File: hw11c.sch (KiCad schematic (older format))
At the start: 68 parts, among them Q1 KX-7_12MHZ, SW1 BUTT1, SW2 BUTT2, X1 ~RESET, X10 PIO2.8, X11 PIO1.4, X12 ADC3, X13 PIO0.8, X14 PIO0.9, X15 MAT0, X16 PIO0.6, X17 PIO0.7, X2 SWCLK, X3 SWDIO, X4 SSEL1, X5 SCK1, X6 MISO1, X7 MOSI1, X8 PIO2.6, X9 PIO2.7

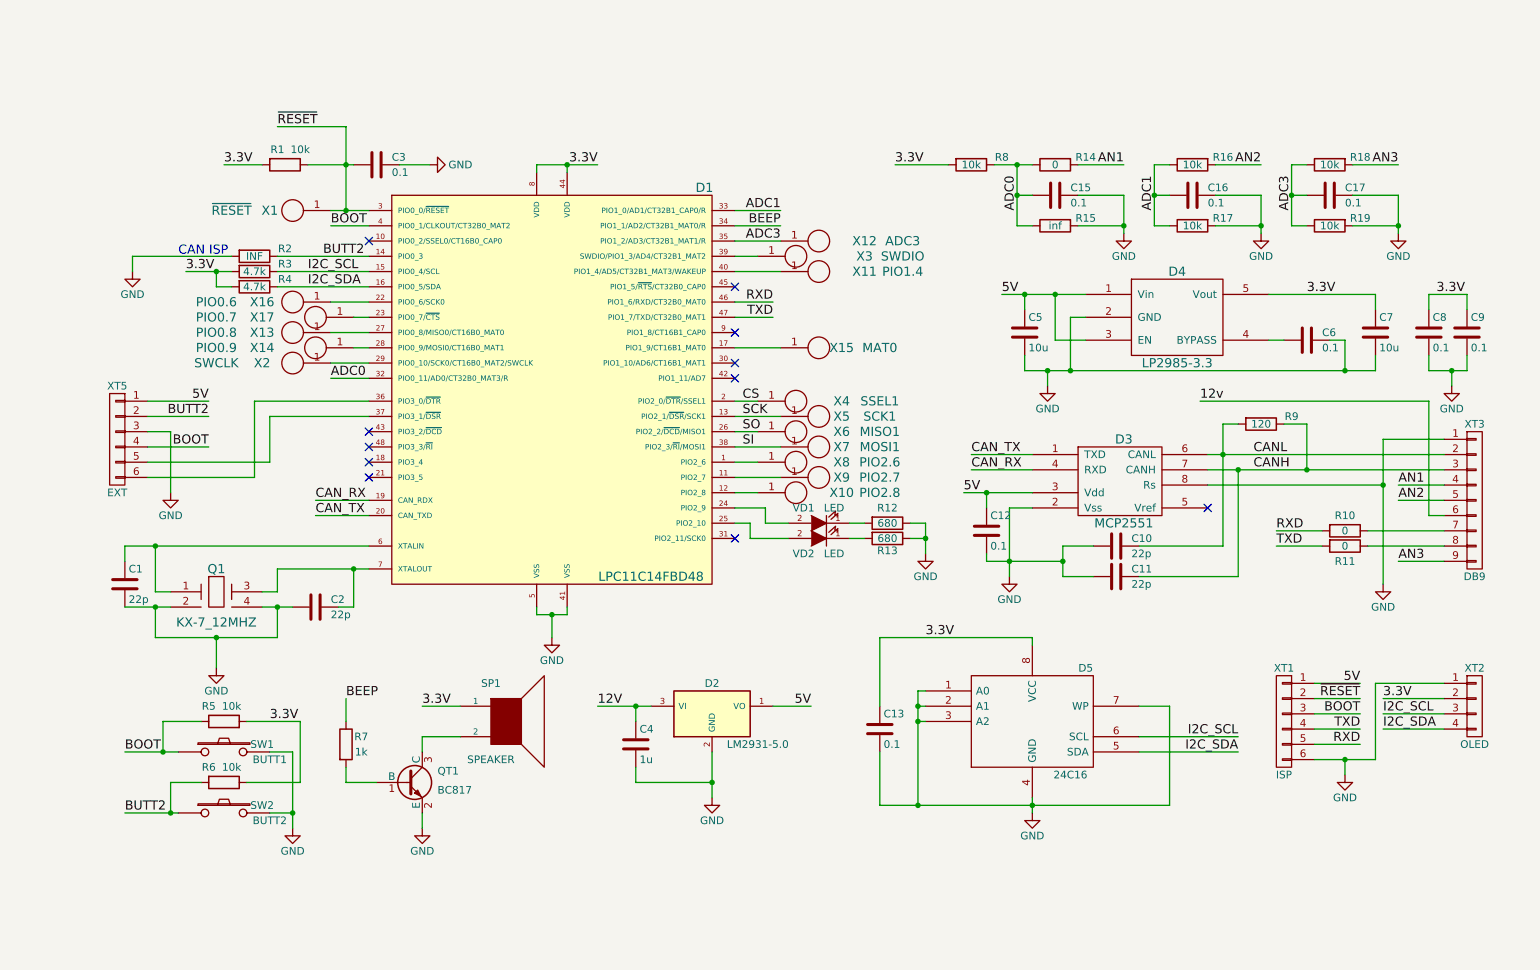
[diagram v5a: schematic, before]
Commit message: Add TJA1055 (Fault-tolerant CAN) on board. This PHY use in some CAN-BODY (comfort bus).
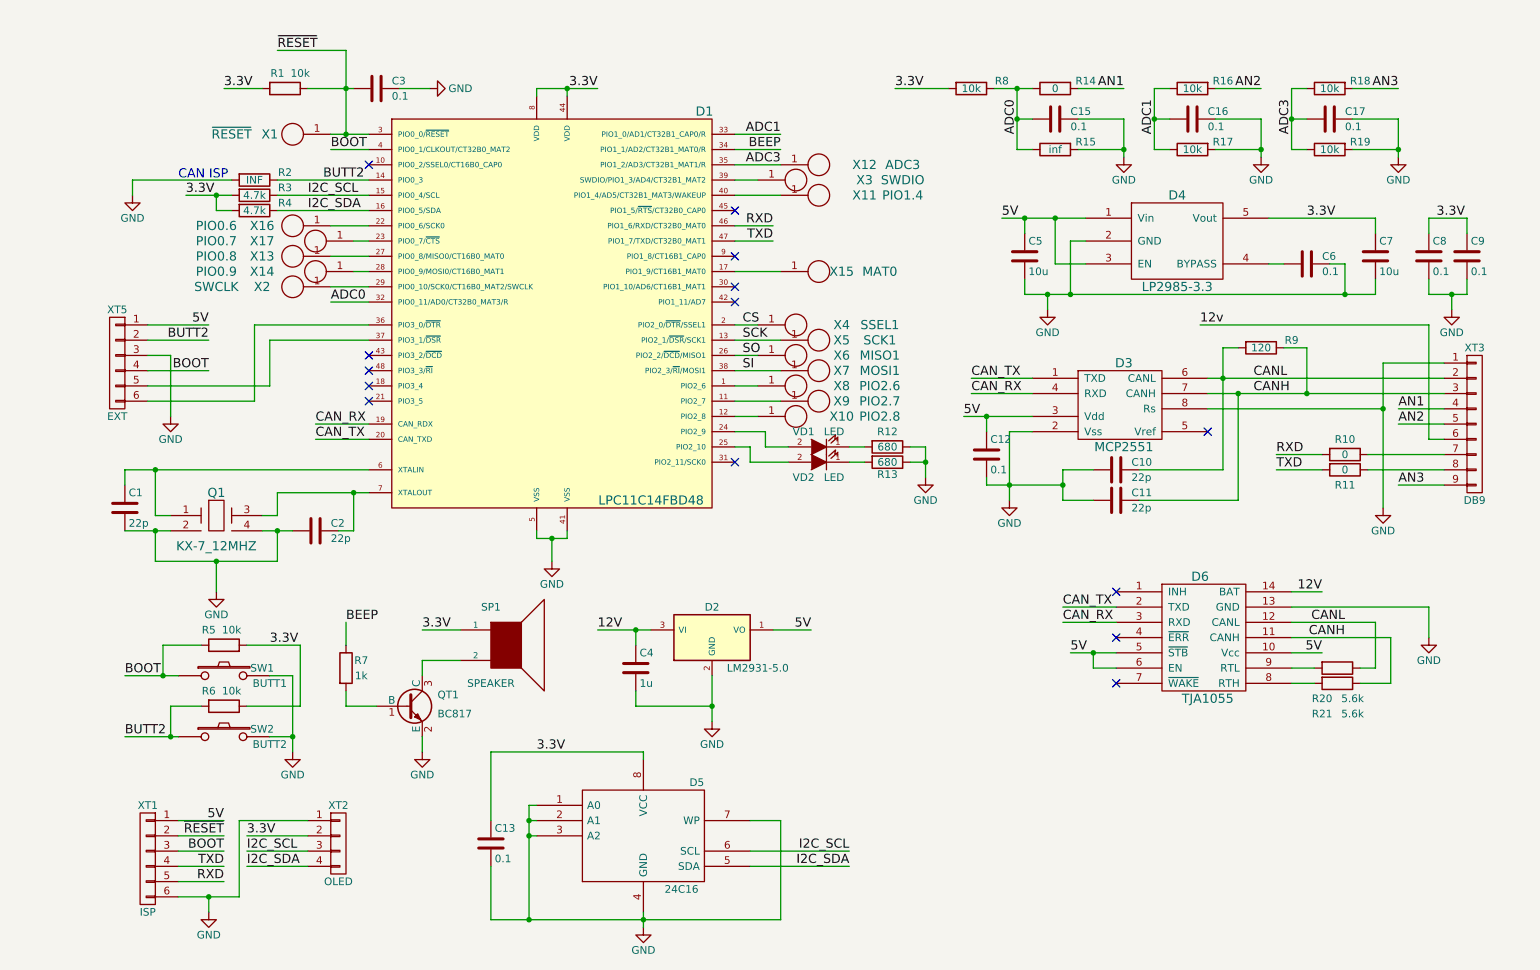
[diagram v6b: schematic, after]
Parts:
- added D6: TJA1055, libs:SOIC-14_N, symbol TJA1055
- added R20, R21: 5.6k, libs:R_0603, symbol R
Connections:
- net 12V: now also D6.14 (BAT)
- net 5V: now also D6.10 (Vcc), D6.5 (~STB), D6.6 (EN)
- net CANH: now also D6.11 (CANH), R21.1
- net CANL: now also D6.12 (CANL), R20.1
- net CAN_RX: now also D6.3 (RXD)
- net CAN_TX: now also D6.2 (TXD)
- net GND: now also D6.13 (GND)
- new net: D6.8 (RTH), R21.2
- new net: D6.9 (RTL), R20.2
- no-connect marks 11 -> 14
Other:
- moved on the sheet: C1, C10, C11, C12, C13, C15, C16, C17, C2, C3, C4, C5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

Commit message: Version 2.1 commit.
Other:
- note added: "Use only one PHY driver: MCP2551 or TJA1055."
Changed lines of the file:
@@
 Rev "4"
 Comp "igorkov.org/bcomp11v2"
-Comment1 "v2.0"
+Comment1 "v2.1"
 Comment2 "igorkov"
 Comment3 ""
@@
 	9000 4750 9200 4750
 Wire Wire Line
-	7850 5150 7550 5150
-Text Label 7550 5150 0    60   ~ 0
+	7500 5150 7850 5150
+Text Label 7500 5150 0    60   ~ 0
 5V
 Wire Wire Line
@@
 NoConn ~ 7850 5050
 NoConn ~ 7850 5350
+Text Notes 7600 5700 0    60   ~ 0
+Use only one PHY driver: MCP2551 or TJA1055.
 $EndSCHEMATC

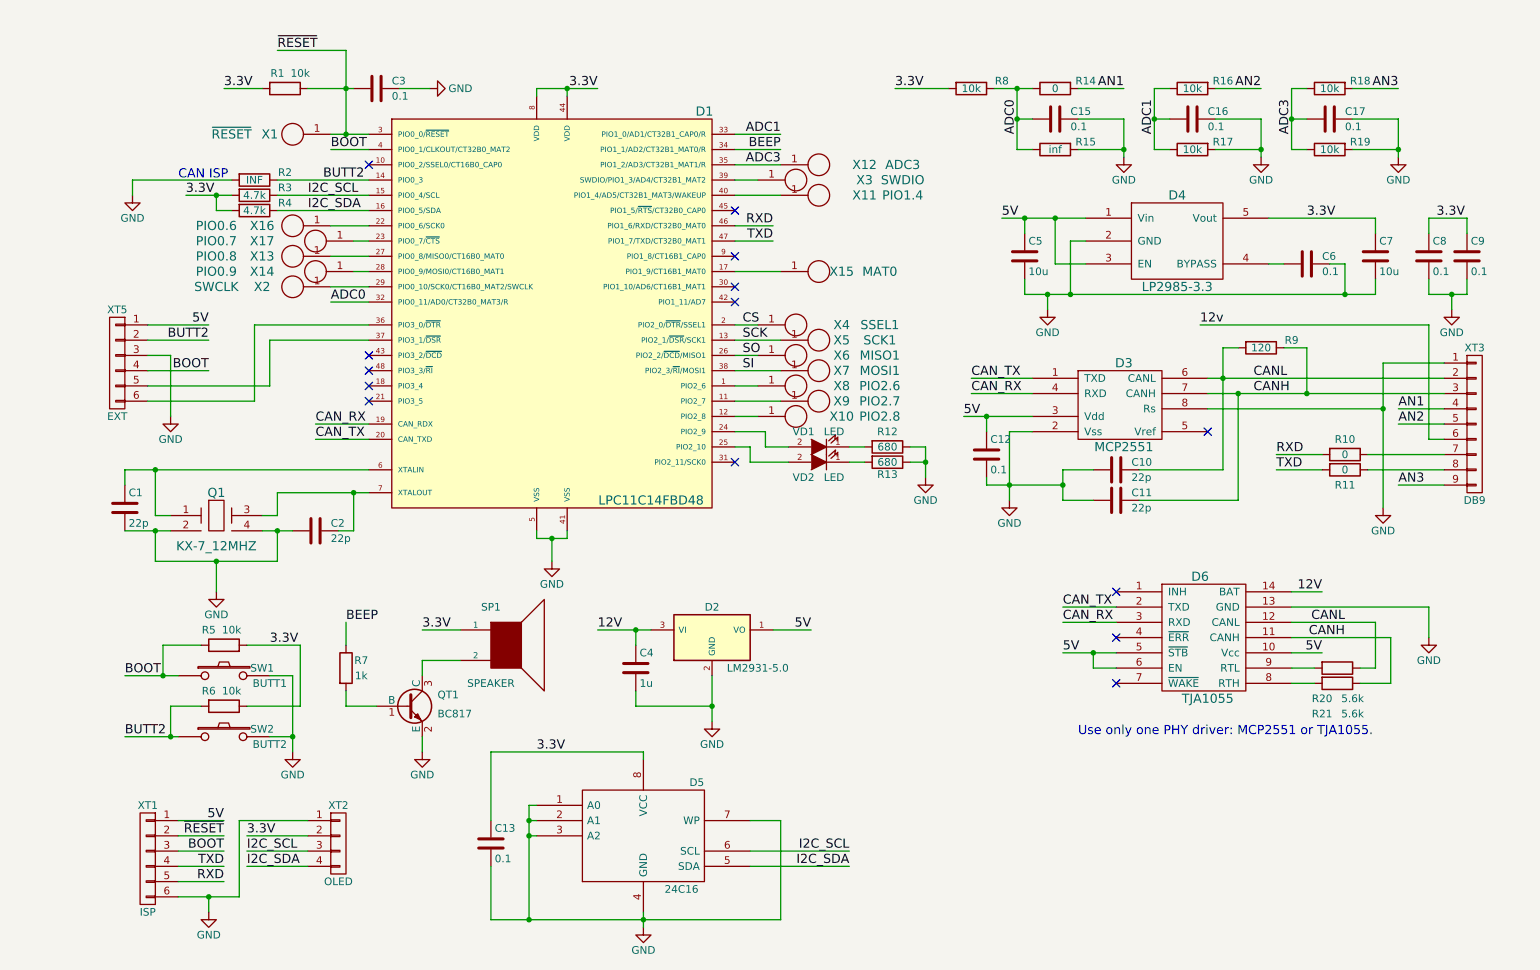
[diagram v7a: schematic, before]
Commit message: Add open-drain outs (shared with analog input). Version 2.3.
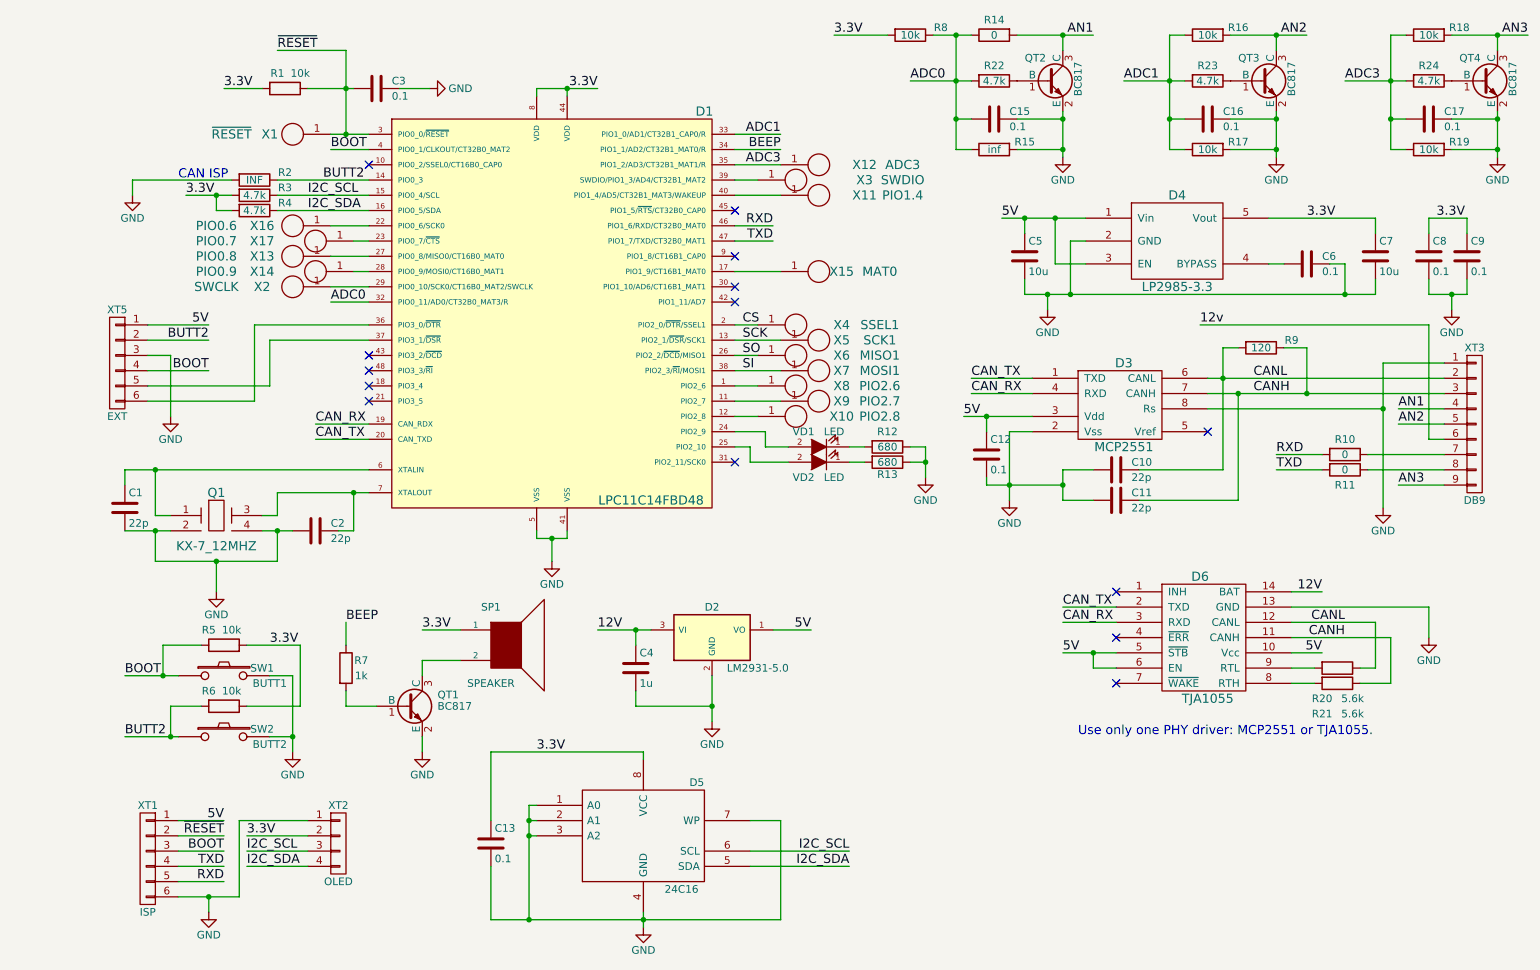
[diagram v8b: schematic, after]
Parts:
- added QT2, QT3, QT4: BC817, libs:SOT-23, symbol BC817-40
- added R22, R23, R24: 4.7k, libs:R_0603, symbol R
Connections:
- net ADC0: now also R22.2
- net ADC1: now also R23.2
- net ADC3: now also R24.2
- net AN1: now also QT2.3 (C)
- net AN2: now also QT3.3 (C)
- net AN3: now also QT4.3 (C)
- net GND: now also QT2.2 (E), QT3.2 (E), QT4.2 (E)
- new net: QT2.1 (B), R22.1
- new net: QT3.1 (B), R23.1
- new net: QT4.1 (B), R24.1
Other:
- moved on the sheet: C15, C16, C17, R14, R15, R16, R17, R18, R19, R8
